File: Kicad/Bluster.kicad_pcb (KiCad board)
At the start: 2 copper layers, 22.9 x 86.4 mm, 10 parts, among them J1 Buster, J2 Buster, U1 XC9572XL, U2 TC1262-3.3V

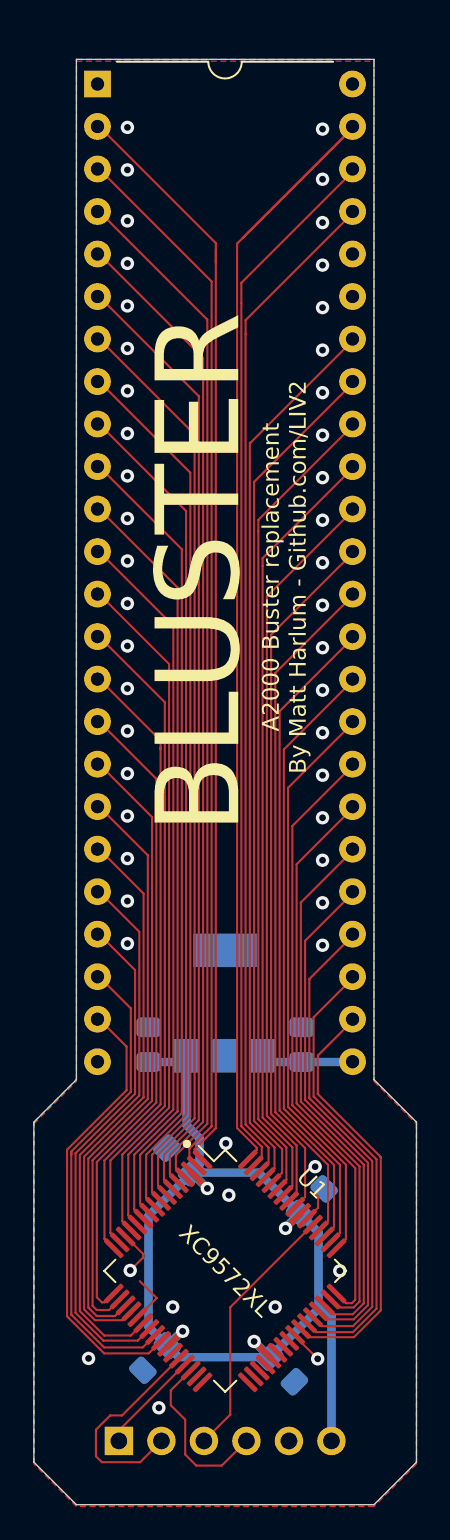
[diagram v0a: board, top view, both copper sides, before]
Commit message: Re-do PCB to fit within standard DIP footprint
Fixes #1
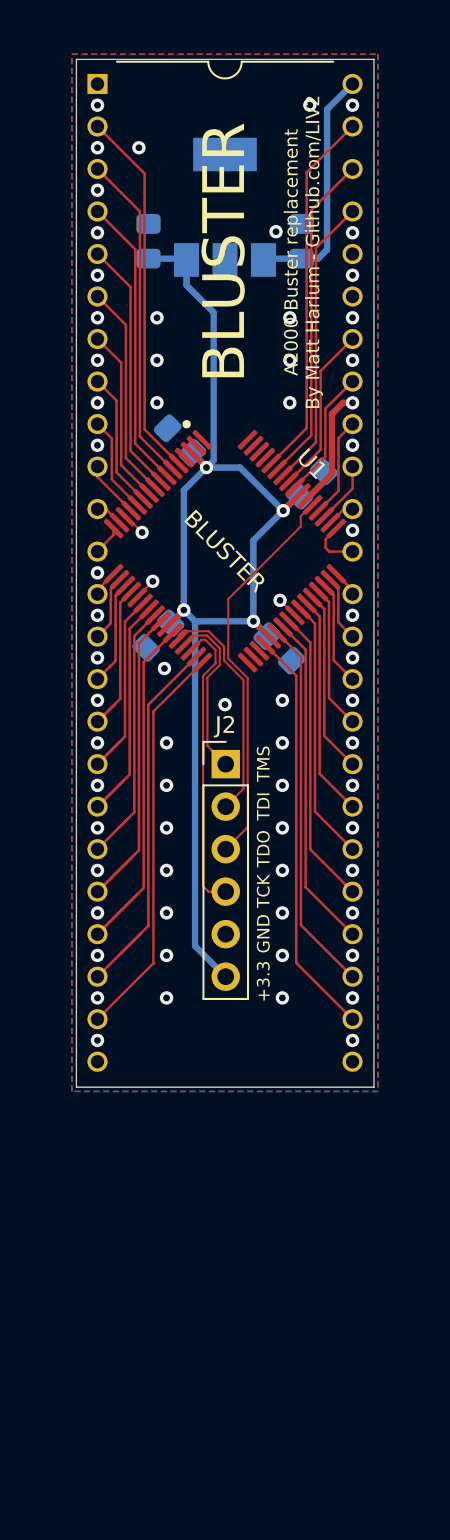
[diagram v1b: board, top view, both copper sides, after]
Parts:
- J2: moved to F.Cu
- U1: value XC9572XL -> BLUSTER
- moved C5 48.0 mm to (173.5, 49.0)
- moved C6 48.0 mm to (164.3, 49.0)
- moved U2 47.6 mm to (168.9, 46.9)
- moved C4 43.2 mm to (164.9, 72.5)
- moved C1 43.1 mm to (172.2, 73.3)
- moved C3 43.0 mm to (166.2, 60.9)
- moved U1 43.0 mm to (168.9, 67.5)
- moved C2 42.9 mm to (174.1, 63.4)
- moved J2 40.9 mm to (168.9, 80.2), turned to 0 degrees
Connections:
- J1 pad 25: +5V -> Net-(J1-Pad25)
- J1 pad 48: Net-(J1-Pad48) -> +5V
- U1 pad 1: /~BG1 -> Net-(U1-Pad1)
- U1 pad 10: /~BR4 -> /~BR1
- U1 pad 11: /~BR5 -> /~BR2
- U1 pad 12: /~SLAVE1 -> /~BR3
- U1 pad 13: /~SLAVE2 -> /~BR4
- U1 pad 15: /~SLAVE3 -> /~BR5
- U1 pad 16: /~SLAVE4 -> /~SLAVE1
- U1 pad 17: /~SLAVE5 -> /~SLAVE2
- U1 pad 18: /~BG -> /~SLAVE3
- U1 pad 19: /~CDAC -> /~SLAVE4
- U1 pad 2: /~BG2 -> Net-(U1-Pad2)
- U1 pad 20: /C1 -> /~SLAVE5
- U1 pad 22: /C3 -> /~BG
- U1 pad 23: /~C2 -> /~CDAC
- U1 pad 24: /~C4 -> /C1
- U1 pad 25: /GBG -> /C3
- U1 pad 27: Net-(U1-Pad27) -> /~C2
- U1 pad 31: Net-(U1-Pad31) -> /~C4
- U1 pad 32: Net-(U1-Pad32) -> /GBG
- U1 pad 36: Net-(U1-Pad36) -> /~BEER
- U1 pad 38: Net-(U1-Pad38) -> /~BR
- U1 pad 39: Net-(U1-Pad39) -> /~CBR
- U1 pad 4: /~BG3 -> Net-(U1-Pad4)
- U1 pad 40: Net-(U1-Pad40) -> /~CBG
- U1 pad 42: /~BEER -> /~A19
- U1 pad 43: /~BR -> /~A20
- U1 pad 44: /~CBR -> /~A21
- U1 pad 45: /~CBG -> /~A22
- U1 pad 46: /~A19 -> /~A23
- U1 pad 47: /~A20 -> /READ
- U1 pad 48: /~A21 -> /~AS
- U1 pad 49: /~A22 -> /~LDS
- U1 pad 5: /~BG4 -> /~BG1
- U1 pad 50: /~A23 -> /~UDS
- U1 pad 51: /READ -> /~BOSS
- U1 pad 52: /~AS -> /~OVR
- U1 pad 56: /~LDS -> /~OWN
- U1 pad 57: /~UDS -> /~RST
- U1 pad 58: /~BOSS -> /D2P
- U1 pad 59: /~OVR -> /~DBOE
- U1 pad 6: /~BG5 -> /~BG2
- U1 pad 60: /~OWN -> /DOE
- U1 pad 61: /~RST -> Net-(U1-Pad61)
- U1 pad 62: /D2P -> Net-(U1-Pad62)
- U1 pad 63: /~DBOE -> Net-(U1-Pad63)
- U1 pad 64: /DOE -> Net-(U1-Pad64)
- U1 pad 7: /~BR1 -> /~BG3
- U1 pad 8: /~BR2 -> /~BG4
- U1 pad 9: /~BR3 -> /~BG5
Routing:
- net /DOE: track 74.7 -> 22.1 mm
- net /~BR4: track 47.9 -> 3.48 mm
- net /~BR3: track 50.1 -> 5.82 mm
- net /~BR2: track 52.4 -> 8.15 mm
- net /~BR1: track 54.6 -> 10.5 mm
- net /~BG5: track 56.9 -> 12.8 mm
- net /~BR5: track 45.6 -> 1.65 mm
- net /~BG4: track 59.1 -> 15.1 mm
- net /~BG1: track 66.1 -> 22.1 mm
- net /~BG3: track 61.4 -> 17.5 mm
- net /~OWN: track 51.3 -> 7.74 mm
- net /~RST: track 53.5 -> 10.1 mm
- net /D2P: track 60.8 -> 17.5 mm
- net /~DBOE: track 63.1 -> 19.8 mm
- net /~BG2: track 63.0 -> 19.8 mm
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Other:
- board size 22.9 x 86.4 mm -> 17.8 x 61.4 mm
- rule via_min_size: 0.4 -> 0.45
- board text added: "REV B OCT 2021"
- board text removed: "REV A JAN 2021"

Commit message: Rev C
* Change LDO to LM1117
* Route extra pins to allow use for Gary
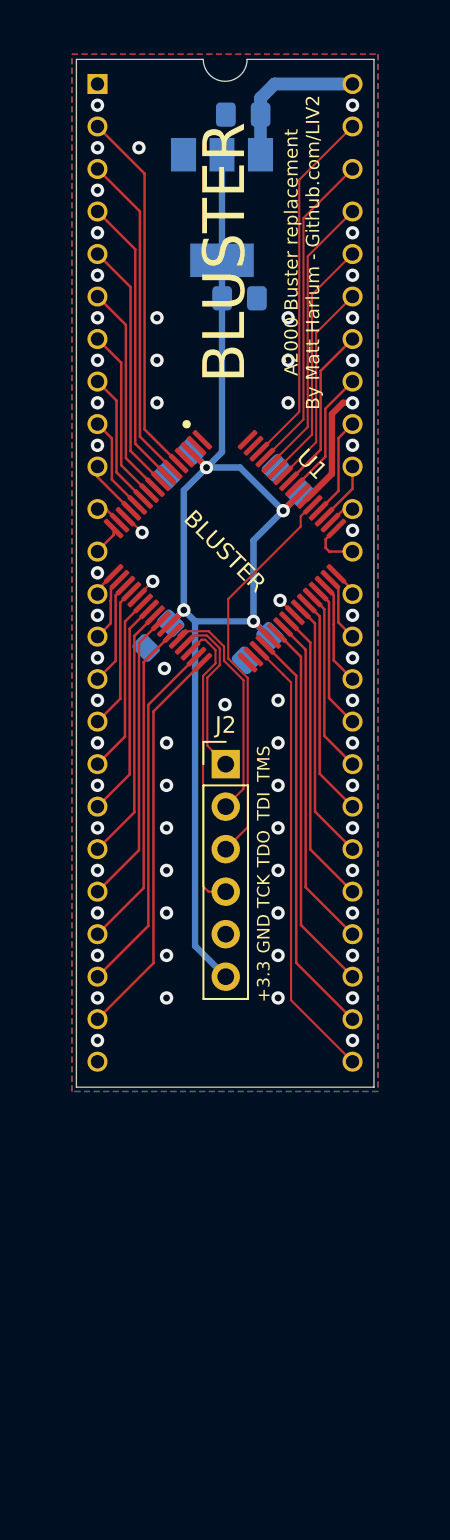
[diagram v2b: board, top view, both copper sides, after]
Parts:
- U2: value TC1262-3.3V -> LM1117-3.3
- moved C5 8.33 mm to (170.0, 41.4), turned to 180 degrees
- moved C6 6.42 mm to (169.8, 52.4), turned to 0 degrees
- moved C2 1.44 mm to (172.7, 63.2), turned to 135 degrees
- moved C3 1.39 mm to (166.2, 62.3), turned to -135 degrees
- moved C1 1.29 mm to (170.9, 73.3), turned to -135 degrees
- moved U2 0.18 mm to (168.7, 47.0), turned to -90 degrees
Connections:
- net /~A19 renamed /~{A19}
- net /~A20 renamed /~{A20}
- net /~A21 renamed /~{A21}
- net /~A22 renamed /~{A22}
- net /~A23 renamed /~{A23}
- net /~AS renamed /~{AS}
- net /~BEER renamed /~{BEER}
- net /~BG renamed /~{BG}
- net /~BG1 renamed /~{BG1}
- net /~BG2 renamed /~{BG2}
- net /~BG3 renamed /~{BG3}
- net /~BG4 renamed /~{BG4}
- net /~BG5 renamed /~{BG5}
- net /~BOSS renamed /~{BOSS}
- net /~BR renamed /~{BR}
- net /~BR1 renamed /~{BR1}
- net /~BR2 renamed /~{BR2}
- net /~BR3 renamed /~{BR3}
- net /~BR4 renamed /~{BR4}
- net /~BR5 renamed /~{BR5}
- net /~C2 renamed /~{C2}
- net /~C4 renamed /~{C4}
- net /~CBG renamed /~{CBG}
- net /~CBR renamed /~{CBR}
- net /~CDAC renamed /~{CDAC}
- net /~LDS renamed /~{LDS}
- net /~OVR renamed /~{OVR}
- net /~OWN renamed /~{OWN}
- net /~RST renamed /~{RST}
- net /~SLAVE1 renamed /~{SLAVE1}
- net /~SLAVE2 renamed /~{SLAVE2}
- net /~SLAVE3 renamed /~{SLAVE3}
- net /~SLAVE4 renamed /~{SLAVE4}
- net /~SLAVE5 renamed /~{SLAVE5}
- net /~UDS renamed /~{UDS}
- J1 pad 25: Net-(J1-Pad25) -> /25
- J1 pad 43: Net-(J1-Pad43) -> /TEST
- J1 pad 44: Net-(J1-Pad44) -> /PTEST
- J1 pad 46: /~DBOE -> /~{DBOE}
- U1 pad 1: Net-(U1-Pad1) -> unconnected-(U1-Pad1)
- U1 pad 2: Net-(U1-Pad2) -> unconnected-(U1-Pad2)
- U1 pad 33: Net-(U1-Pad33) -> unconnected-(U1-Pad33)
- U1 pad 34: Net-(U1-Pad34) -> unconnected-(U1-Pad34)
- U1 pad 35: Net-(U1-Pad35) -> /25
- U1 pad 4: Net-(U1-Pad4) -> unconnected-(U1-Pad4)
- U1 pad 58: /D2P -> /TEST
- U1 pad 59: /~DBOE -> /PTEST
- U1 pad 60: /DOE -> /D2P
- U1 pad 61: Net-(U1-Pad61) -> /~{DBOE}
- U1 pad 62: Net-(U1-Pad62) -> /DOE
- U1 pad 63: Net-(U1-Pad63) -> unconnected-(U1-Pad63)
- U1 pad 64: Net-(U1-Pad64) -> unconnected-(U1-Pad64)
- U2 pad 1: +5V -> GND
- U2 pad 2: GND -> +3V3
- U2 pad 3: +3V3 -> +5V
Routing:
- net /25: track 0.00 -> 26.9 mm
- net /~DBOE: track 19.8 -> 0.00 mm
- net /~{DBOE}: track 0.00 -> 19.4 mm
- net /PTEST: track 0.00 -> 14.7 mm
- net /TEST: track 0.00 -> 12.4 mm
- net +5V: track 14.6 -> 9.24 mm
- net +3V3: track 74.7 -> 78.3 mm
- net /~{C2}: track 23.2 -> 19.9 mm
- net /C3: track 20.7 -> 17.7 mm
- net /~{CDAC}: track 15.3 -> 13.1 mm
- net /~{BG}: track 12.6 -> 10.7 mm
- net /~{C4}: track 23.3 -> 21.6 mm
- net /~{SLAVE5}: track 10.1 -> 8.61 mm
- net /C1: track 16.2 -> 15.4 mm
- net GND: vias 68 -> 67
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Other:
- outline, holes or cut-outs redrawn
- net class Default removed
- board text added: "REV C JAN 2022"
- board text removed: "REV B OCT 2021"
